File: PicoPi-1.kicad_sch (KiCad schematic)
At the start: 45 parts, among them J1 Pi Pico, J2 P1, J3 P2, J4 Conn_01x02, J5 Conn_01x02

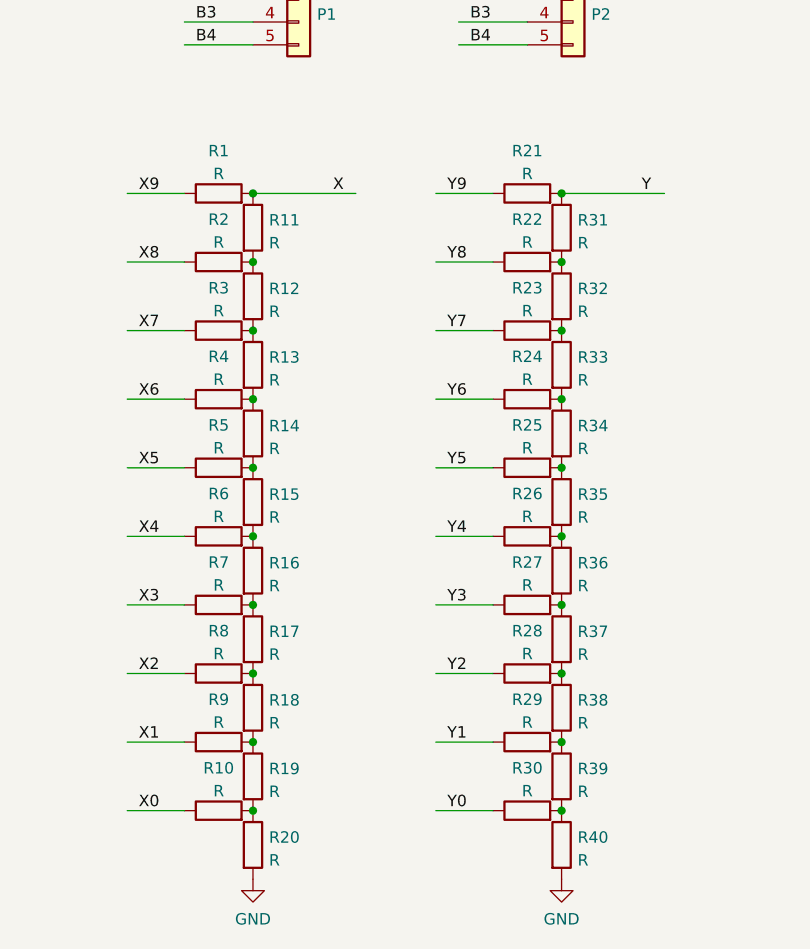
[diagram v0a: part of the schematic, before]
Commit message: Spacewar works with X/Y output
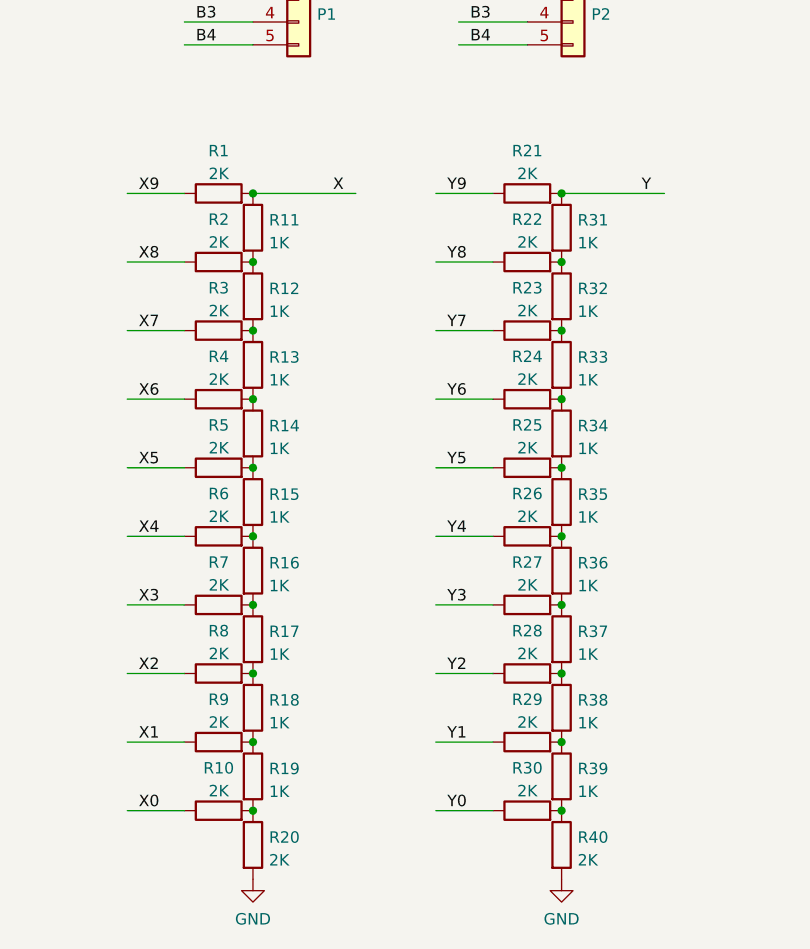
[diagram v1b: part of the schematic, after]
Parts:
- R1, R10, R2, R20, R21, R22, R23, R24, R25, R26, R27, R28, R29, R3, R30, R4, R40, R5, R6, R7, R8, R9: value R -> 2K
- R11, R12, R13, R14, R15, R16, R17, R18, R19, R31, R32, R33, R34, R35, R36, R37, R38, R39: value R -> 1K
